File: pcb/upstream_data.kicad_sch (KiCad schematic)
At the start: 0 parts

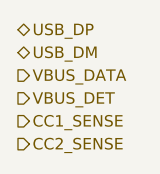
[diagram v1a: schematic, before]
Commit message: take the CC senses out, and let that simplify what feeds the charger
Asking what the CC senses needed answered the question by deleting them. They
were there so the firmware could learn whether the data port's source offers
more than the USB default, but that buys nothing: the data port's contribution
is capped by intent rather than by what the source offers, because it exists so
a board with no battery and no charger can still be reflashed, not as a way to
run the ports. Removing them takes two pins, four resistors and a clamp
question off the board, and avoids a subtler risk -- any divider across CC sits
in parallel with the termination that tells the source what we are, and shifting
that is worse than not knowing.

Which collapses the ORing. A prioritised controller with external FETs was
specified because two sources meet at the charger and 9 V must never reach the
data port. A path limited to the USB default can afford a Schottky instead: it
blocks reverse without being told, costs about a fifth of a watt on a path that
is rarely used, and the charger's buck-boost input does not care about the drop.
The power port stays direct, on the condition that the sink opens its own output
switch when nothing is attached. The charger then tells its two sources apart by
their voltage, which it already measures, so the per-source limit is firmware
work rather than a board question.

The 9 V request is recorded from the driver in this codebase that already does
it on hardware: select the profile, then issue go, in that order, because go
acts on whatever the selection register holds at that instant -- and every
register written as a strictly framed two-byte transaction, because the
repeated-start form is acknowledged and stores nothing.

One new problem, found rather than closed. The port switch is rated 1.5 A and
goes constant-current near 2.15 A, so it protects the part but does not enforce
the port's budget; four of them could ask the 5 V rail for far more than it is
built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
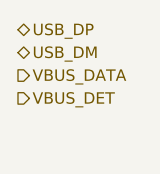
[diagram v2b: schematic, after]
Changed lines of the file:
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@@
-		)
-	)
-	(hierarchical_label "CC2_SENSE"
-		(shape output)
-		(at 60 52.7 0)
-		(effects
-			(font
-				(size 1.27 1.27)
-			)
-			(justify left)
 		)
 	)
@@
 		(effects
 			(font
-				(size 1.27 1.27)
-			)
-			(justify left)
-		)
-	)
-	(hierarchical_label "CC1_SENSE"
-		(shape output)
-		(at 60 50.16 0)
-		(effects
-			(font

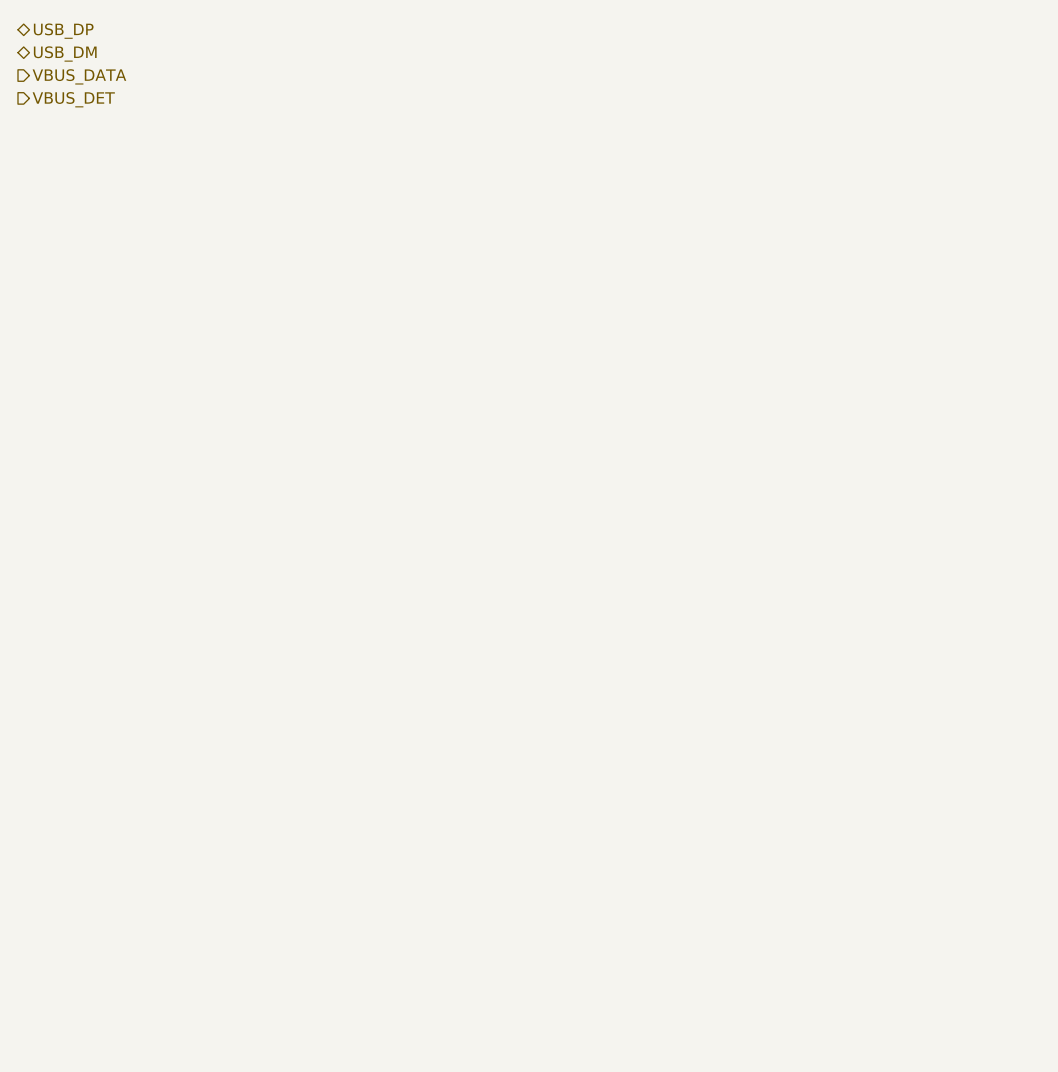
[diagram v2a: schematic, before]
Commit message: draw the data port, and let its pinout answer an open question
The receptacle, the terminations that tell a source what we are, the protection
array, the sense divider the firmware reads to know a host is there, and the
diode through which the rail takes its capped contribution. Both halves of each
data pair are tied, which is what lets the cable go in either way up -- four pin
points, not two, and the netlist is the only place that shows it was done.

Reading the PD sink's pinout to draw the other upstream sheet answered a
question that was down as needing the datasheet by eye. It has no internal
output switch to open: it brings out a gate drive for an external FET. So the
blocking that keeps the data port from back-driving an exposed connector is ours
to design rather than someone else's arrangement to trust, and the open item
becomes an orientation choice. The same pinout shows the requested voltage and
current are resistor-settable as well as addressable, so the profile has a
hardware default before any firmware runs -- worth having on a board whose
firmware is the thing being updated.

The power sheet is NOT drawn, and deliberately. Its three converters each need
numbers this toolchain cannot read: which resistor sets the charger's current
programming against its input-limit pin, and how to tell the boost's feedback
divider apart from its current-limit and frequency resistors. The vendor
publishes both with the pin tables and design equations in a form that extracts
at four and thirty per cent. The topology is understood; the values are not, and
a wrong number in the supply is expensive, so it is recorded as needing a human
with the PDF open rather than drawn from inference.

Co-Authored-By: Claude Opus 5 (1M context) <noreply@anthropic.com>
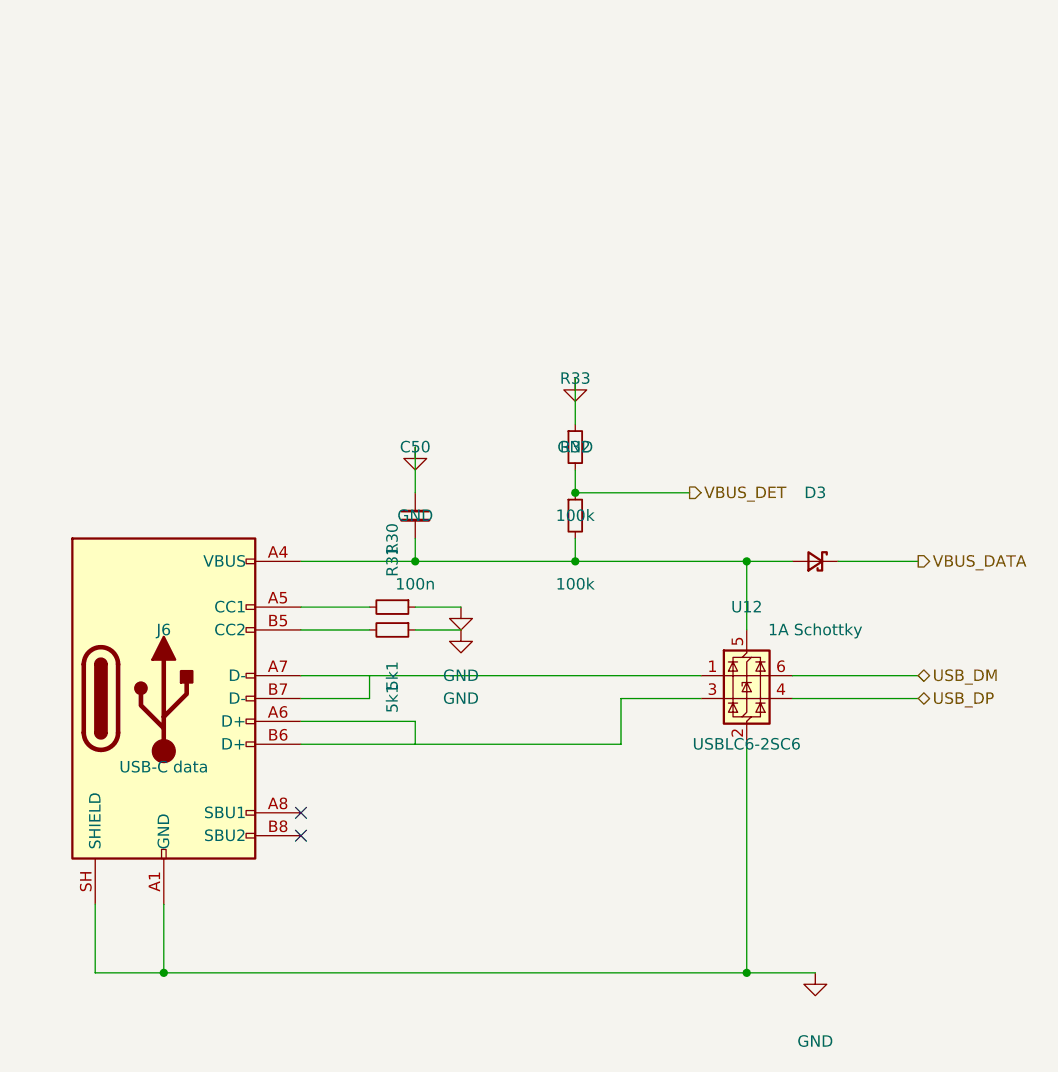
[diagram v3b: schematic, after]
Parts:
- added C50: 100n, symbol Device:C_Small
- added D3: 1A Schottky, symbol Device:D_Schottky_Small
- added J6: USB-C data, symbol Connector:USB_C_Receptacle_USB2.0_16P
- added R30, R31: 5k1, symbol Device:R_Small
- added R32, R33: 100k, symbol Device:R_Small
- added U12: USBLC6-2SC6, symbol Power_Protection:USBLC6-2SC6
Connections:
- net USB_DM: now also U12.6 (I/O1)
- net USB_DP: now also U12.4 (I/O2)
- net VBUS_DATA: now also D3.1 (K)
- net VBUS_DET: now also R32.1, R33.2
- new net: J6.A5 (CC1), R30.2
- new net: J6.B5 (CC2), R31.2
- new net: C50.2, D3.2 (A), J6.A4 (VBUS), J6.A9 (VBUS), J6.B4 (VBUS), J6.B9 (VBUS), R32.2, U12.5 (VBUS)
- new net: J6.A6 (D+), J6.B6 (D+), U12.3 (I/O2)
- new net: J6.A7 (D-), J6.B7 (D-), U12.1 (I/O1)
- new net GND: C50.1, J6.A1 (GND), J6.A12 (GND), J6.B1 (GND), J6.B12 (GND), J6.SH (SHIELD), R30.1, R31.1, R33.1, U12.2 (GND)
- no-connect marks 0 -> 2

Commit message: fit both input switches, as a patch over the sheets as they stand
A pair of transistors on each upstream port, wired into the sheets that already exist rather than
by regenerating them, so the hand layout is untouched: every removal was matched to exactly one
object by the coordinates it sat at, and the new work was appended.

The input stage now reads as three nets where it read as one. Each feed arrives on its own net and
stays there; they meet only through the switches, on the node the input capacitors and the charger
share. The detect pins moved to the connector side of their own pair, the drivers stopped being
tied to ground, and the diode came out of the data port's sheet. The pairs reach the charger by
name rather than by wires dragged across the sheet, which is what kept this a patch. That also
retires a long-standing complaint from the rules check: the two feeds used to be one net wearing
two names, so the project is down one known violation rather than up any.

Two faults in the drawing turned up on the way, and neither was an error the rules check can see.

The diode the switch replaced was pointing the wrong way -- cathode to the connector -- so it would
have blocked the data port from contributing anything and conducted the charger's rail back out to
whatever was plugged in, which is the exact failure it was placed to prevent. It is gone now, but
it would have reached a board if the switch had not displaced it.

And the three input capacitors each had a wire bridging their own two pins, shorting the charger's
input to ground. That is not in the committed sheet and not something this change introduced; a
part moved in the editor can be left bridged by the wire it was sitting on. The bridges are
removed. Neither fault is electrically illegal, which is why the rules check passes them: a bridged
part is just a net. Both came out of reading the connection list instead of the picture, and the
scan worth repeating after any hand edit is now written down -- doe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
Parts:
- removed D3: 1A Schottky, symbol Device:D_Schottky_Small
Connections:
- net VBUS_DATA: now also C50.2, J6.A4 (VBUS), J6.A9 (VBUS), J6.B4 (VBUS), J6.B9 (VBUS), R32.2, U12.5 (VBUS)
